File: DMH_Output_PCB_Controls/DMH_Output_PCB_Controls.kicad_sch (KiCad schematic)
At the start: 10 parts, among them J1 TS_Jack_6.35mm_Sw, J2 TS_Jack_6.35mm_Sw, J200 IDC_02x08, J3 TRS Jack 6.35mm, J4 TRS Jack 6.35mm, J5 TRS Jack 6.35mm, J6 TS_Jack_6.35mm_Sw, J7 TS_Jack_6.35mm_Sw, J8 TS_Jack_6.35mm_Sw, J9 TS_Jack_6.35mm_Sw

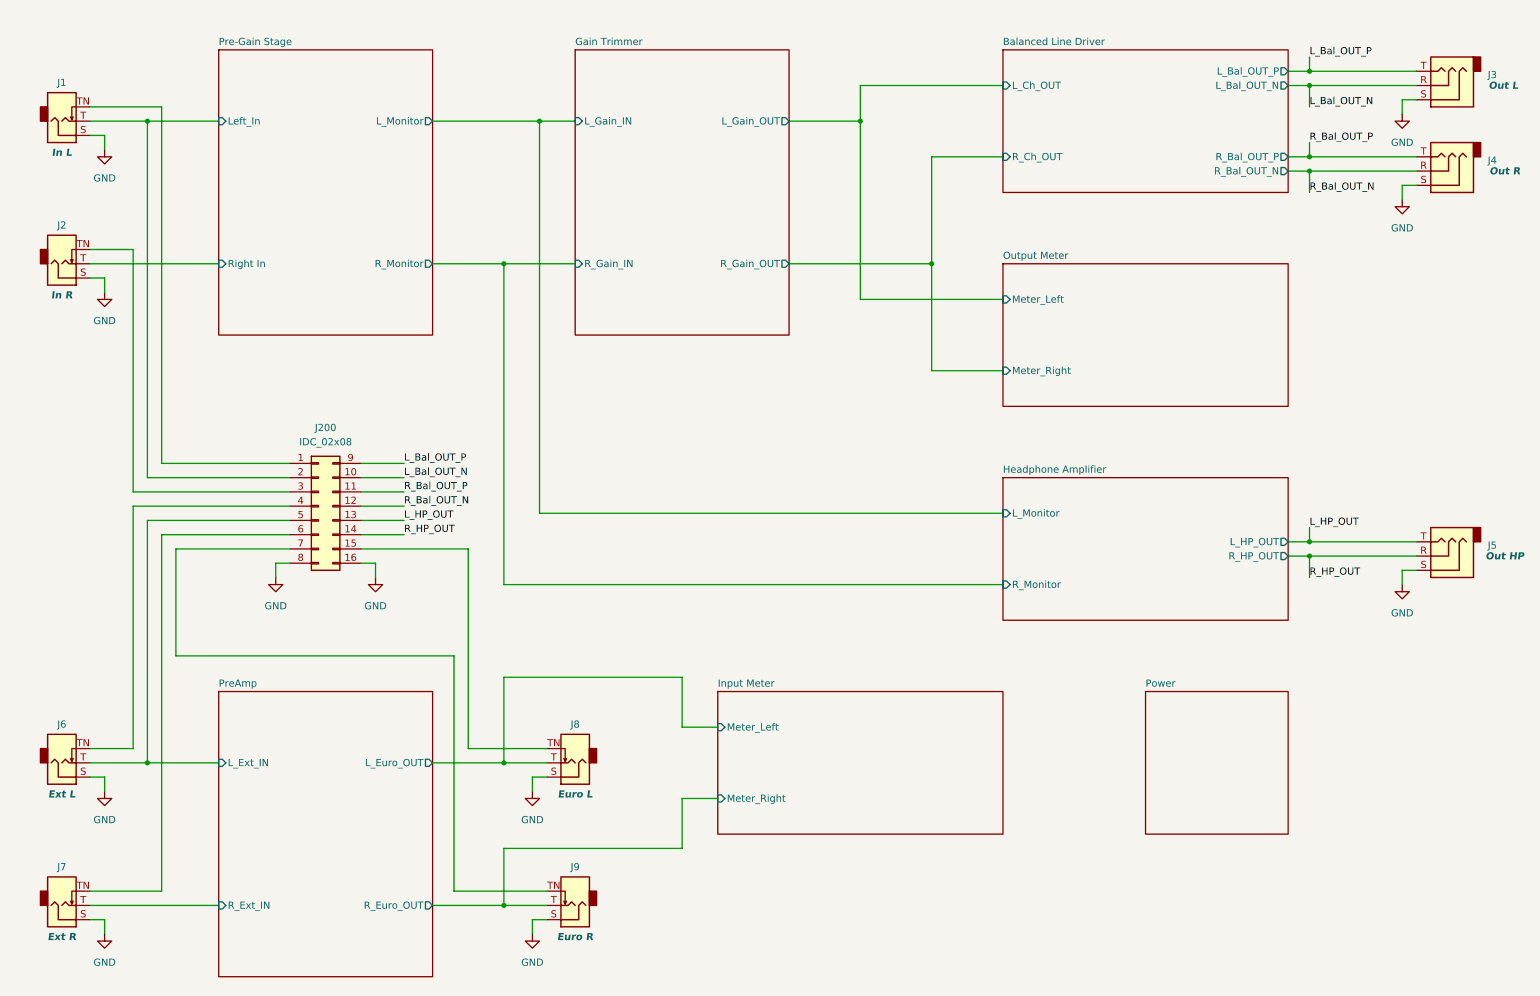
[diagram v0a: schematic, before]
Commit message: Controls PCB placement ongoing
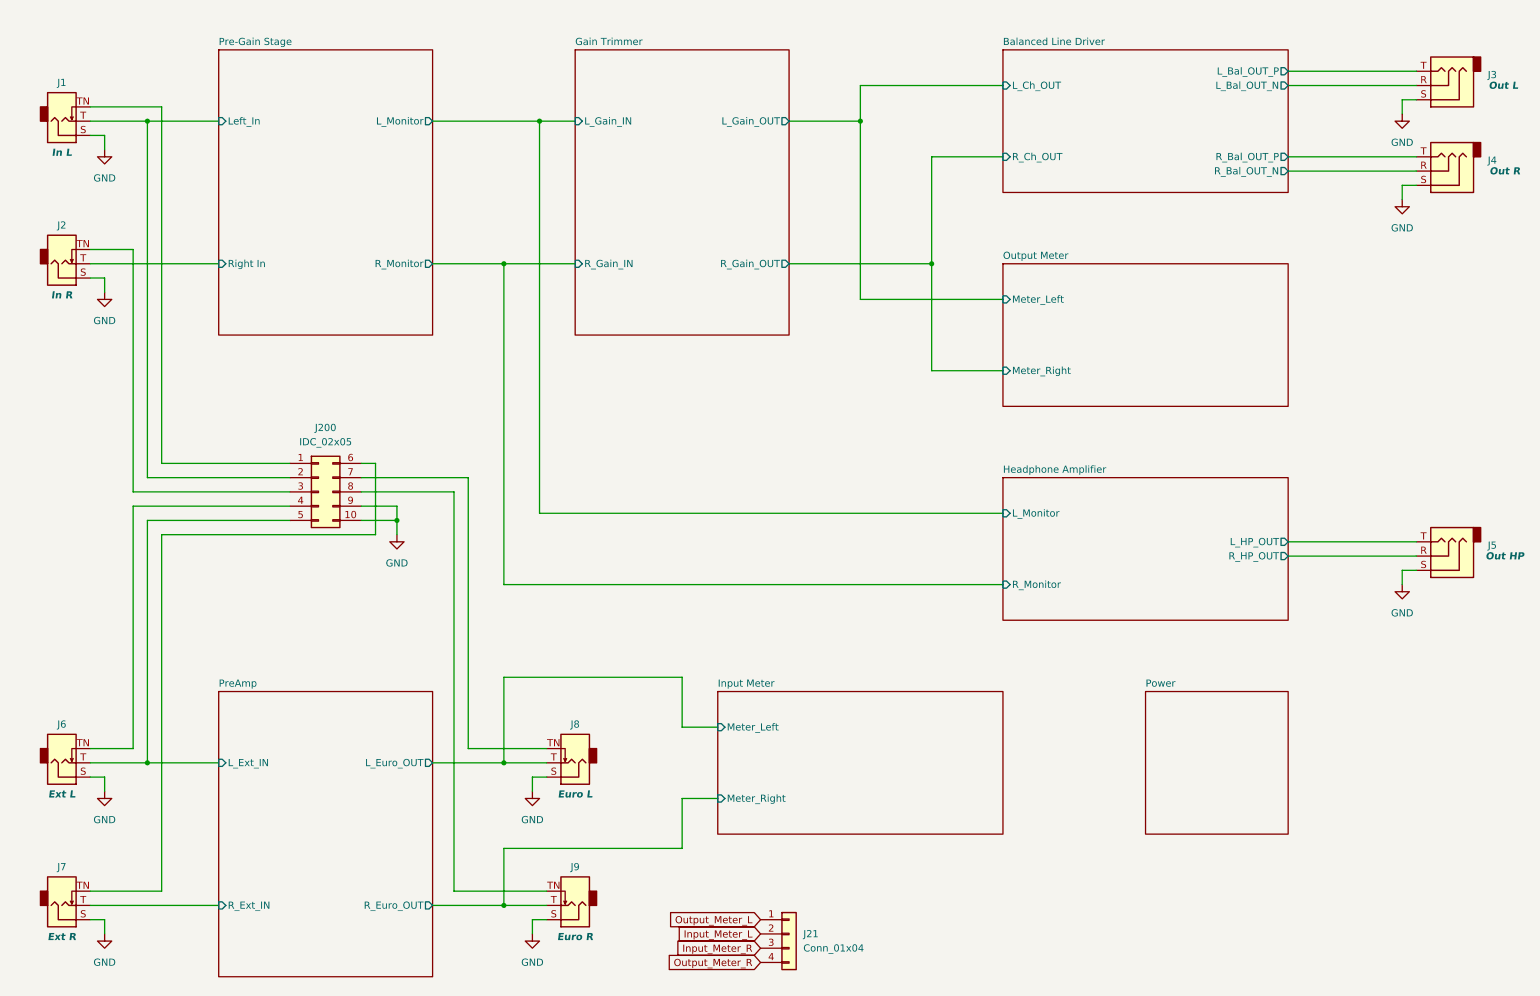
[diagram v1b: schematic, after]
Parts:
- removed J200: IDC_02x08, SynthStuff:IDC-Header_2x08_P2.54mm_Vertical_BackBone, symbol SynthStuff:BackBone_Connector_16Pin
- added J200: IDC_02x05, SynthStuff:IDC-Header_2x05_P2.54mm_Vertical_BackBone, symbol SynthStuff:BackBone_Connector_10Pin
- added J21: Conn_01x04, Connector_PinSocket_2.54mm:PinSocket_1x04_P2.54mm_Vertical, symbol Connector_Generic:Conn_01x04
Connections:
- net GND: now also J200.10 (Pin_10), J200.9 (Pin_9)
- net Pre-Gain Stage/Left_In: now also J200.2 (Pin_2)
- net PreAmp/L_Ext_IN: now also J200.5 (Pin_5)
- net at J8.TN: now also J200.7 (Pin_7)
- net at J2.TN: now also J200.3 (Pin_3)
- net at J7.TN: now also J200.6 (Pin_6)
- net at J6.TN: now also J200.4 (Pin_4)
- net at J1.TN: now also J200.1 (Pin_1)
- net at J9.TN: now also J200.8 (Pin_8)
- net L_Bal_OUT_N renamed Balanced Line Driver/L_Bal_OUT_N
- net L_Bal_OUT_P renamed Balanced Line Driver/L_Bal_OUT_P
- net L_HP_OUT renamed Headphone Amplifier/L_HP_OUT
- net R_Bal_OUT_N renamed Balanced Line Driver/R_Bal_OUT_N
- net R_Bal_OUT_P renamed Balanced Line Driver/R_Bal_OUT_P
- net R_HP_OUT renamed Headphone Amplifier/R_HP_OUT
- new net Input_Meter_L: J21.2 (Pin_2)
- new net Input_Meter_R: J21.3 (Pin_3)
- new net Output_Meter_L: J21.1 (Pin_1)
- new net Output_Meter_R: J21.4 (Pin_4)

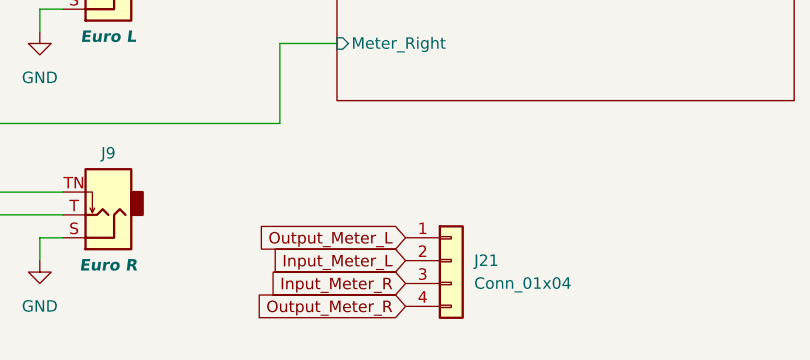
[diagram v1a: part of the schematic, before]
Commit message: Controls PCB routing ongoing
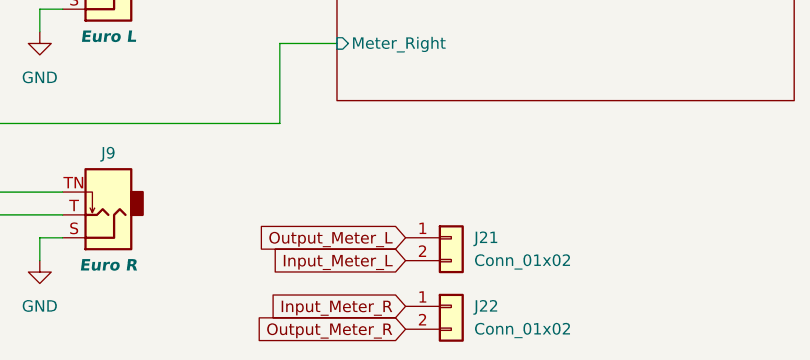
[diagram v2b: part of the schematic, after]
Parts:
- removed J21: Conn_01x04, Connector_PinSocket_2.54mm:PinSocket_1x04_P2.54mm_Vertical, symbol Connector_Generic:Conn_01x04
- added J21, J22: Conn_01x02, Connector_PinSocket_2.54mm:PinSocket_1x02_P2.54mm_Vertical, symbol Connector_Generic:Conn_01x02
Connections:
- net Input_Meter_L: now also J21.2 (Pin_2)
- net Input_Meter_R: now also J22.1 (Pin_1)
- net Output_Meter_L: now also J21.1 (Pin_1)
- net Output_Meter_R: now also J22.2 (Pin_2)
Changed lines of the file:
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@@
 	(global_label "Input_Meter_R"
 		(shape input)
-		(at 147.32 185.42 180)
+		(at 147.32 187.96 180)
 		(fields_autoplaced yes)
 		(effects
@@
 		)
 		(property "Intersheetrefs" "${INTERSHEET_REFS}"
-			(at 131.2116 185.42 0)
+			(at 131.2116 187.96 0)
 			(effects
 				(font
@@
 	(global_label "Output_Meter_R"
 		(shape input)
-		(at 147.32 187.96 180)
+		(at 147.32 190.5 180)
 		(fields_autoplaced yes)
 		(effects
@@
 		)
 		(property "Intersheetrefs" "${INTERSHEET_REFS}"
-			(at 129.7602 187.96 0)
+			(at 129.7602 190.5 0)
 			(effects
 				(font
@@
 	)
 	(symbol
-		(lib_id "Connector_Generic:Conn_01x04")
-		(at 152.4 182.88 0)
-		(unit 1)
-		(exclude_from_sim no)
-		(in_bom yes)
-		(on_board yes)
-		(dnp no)
-		(fields_autoplaced yes)
-		(property "Reference" "J21"
-			(at 154.94 182.8799 0)
-			(effects
-				(font
-					(size 1.27 1.27)
-				)
-				(justify left)
-			)
-		)
-		(property "Value" "Conn_01x04"
-			(at 154.94 185.4199 0)
-			(effects
-				(font
-					(size 1.27 1.27)
-				)
-				(justify left)
-			)
-		)
-		(property "Footprint" "Connector_PinSocket_2.54mm:PinSocket_1x04_P2.54mm_Vertical"
-			(at 152.4 182.88 0)
-			(effects
-				(font
-					(size 1.27 1.27)
-				)
-				(hide yes)
-			)
-		)
-		(property "Datasheet" "~"
-			(at 152.4 182.88 0)
-			(effects
-				(font
-					(size 1.27 1.27)
-				)
-				(hide yes)
-			)
-		)
-		(property "Description" "Generic connector, single row, 01x04, script generated (kicad-library-utils/schlib/autogen/connector/)"
-			(at 152.4 182.88 0)
-			(effects
-				(font
-					(size 1.27 1.27)
-				)
-				(hide yes)
-			)
-		)
-		(pin "2"
-		)
-		(pin "3"
-		)
-		(pin "4"
-		)
-		(pin "1"
-		)
-		(instances
-			(project ""
-				(path "/58f4306d-5387-4983-bb08-41a2313fd315"
-					(reference "J21")
-					(unit 1)
-				)
-			)
-		)
-	)
-	(symbol
 		(lib_id "SynthStuff:TS_Jack_6.35mm_Sw")
 		(at 22.86 63.5 0)
@@
 	)
 	(symbol
+		(lib_id "Connector_Generic:Conn_01x02")
+		(at 152.4 187.96 0)
+		(unit 1)
+		(exclude_from_sim no)
+		(in_bom yes)
+		(on_board yes)
+		(dnp no)
+		(fields_autoplaced yes)
+		(property "Reference" "J22"
+			(at 154.94 187.9599 0)
+			(effects
+				(font
+					(size 1.27 1.27)
+				)
+				(justify left)
+			)
+		)
+		(property "Value" "Conn_01x02"
+			(at 154.94 190.4999 0)
+			(effects
+				(font
+					(size 1.27 1.27)
+				)
+				(justify left)
+			)
+		)
+		(property "Footprint" "Connector_PinSocket_2.54mm:PinSocket_1x02_P2.54mm_Vertical"
+			(at 152.4 187.96 0)
+			(effects
+				(font
+					(size 1.27 1.27)
+				)
+				(hide yes)
+			)
+		)
+		(property "Datasheet" "~"
+			(at 152.4 187.96 0)
+			(effects
+				(font
+					(size 1.27 1.27)
+				)
+				(hide yes)
+			)
+		)
+		(property "Description" "Generic connector, single row, 01x02, script generated (kicad-library-utils/schlib/autogen/connector/)"
+			(at 152.4 187.96 0)
+			(effects
+				(font
+					(size 1.27 1.27)
+				)
+				(hide yes)
+			)
+		)
+		(pin "2"
+		)
+		(pin "1"
+		)
+		(instances
+			(project "DMH_Output_PCB_Controls"
+				(path "/58f4306d-5387-4983-bb08-41a2313fd315"
+					(reference "J22")
+					(unit 1)
+				)
+			)
+		)
+	)
+	(symbol
 		(lib_id "power:GND")
 		(at 261.62 52.07 0)
@@
 					(unit 1)
 				)
+			)
+		)
+	)
+	(symbol
+		(lib_id "Connector_Generic:Conn_01x02")
+		(at 152.4 180.34 0)
+		(unit 1)
+		(exclude_from_sim no)
+		(in_bom yes)
+		(on_board yes)
+		(dnp no)
+		(fields_autoplaced yes)
+		(property "Reference" "J21"
+			(at 154.94 180.3399 0)
+			(effects
+				(font
+					(size 1.27 1.27)
+				)
+				(justify left)
+			)
+		)
+		(property "Value" "Conn_01x02"
+			(at 154.94 182.8799 0)
+			(effects
+				(font
+					(size 1.27 1.27)
+				)
+				(justify left)
+			)
+		)
+		(property "Footprint" "Connector_PinSocket_2.54mm:PinSocket_1x02_P2.54mm_Vertical"
+			(at 152.4 180.34 0)
+			(effects
+				(font
+					(size 1.27 1.27)
+				)
+				(hide yes)
+			)
+		)
+		(property "Datasheet" "~"
+			(at 152.4 180.34 0)
+			(effects
+				(font
+					(size 1.27 1.27)
+				)
+				(hide yes)
+			)
+		)
+		(property "Description" "Generic connector, single row, 01x02, script generated (kicad-library-utils/schlib/autogen/connector/)"
+			(at 152.4 180.34 0)
+			(effects
+				(font
+					(size 1.27 1.27)
+				)
+				(hide yes)
+			)
+		)
+		(pin "2"
+		)
+		(pin "1"
+		)
+		(instances
+			(project ""
+				(path "/58f4306d-5387-4983-bb08-41a2313fd315"
+					(reference "J21")
+					(unit 1)
+				)

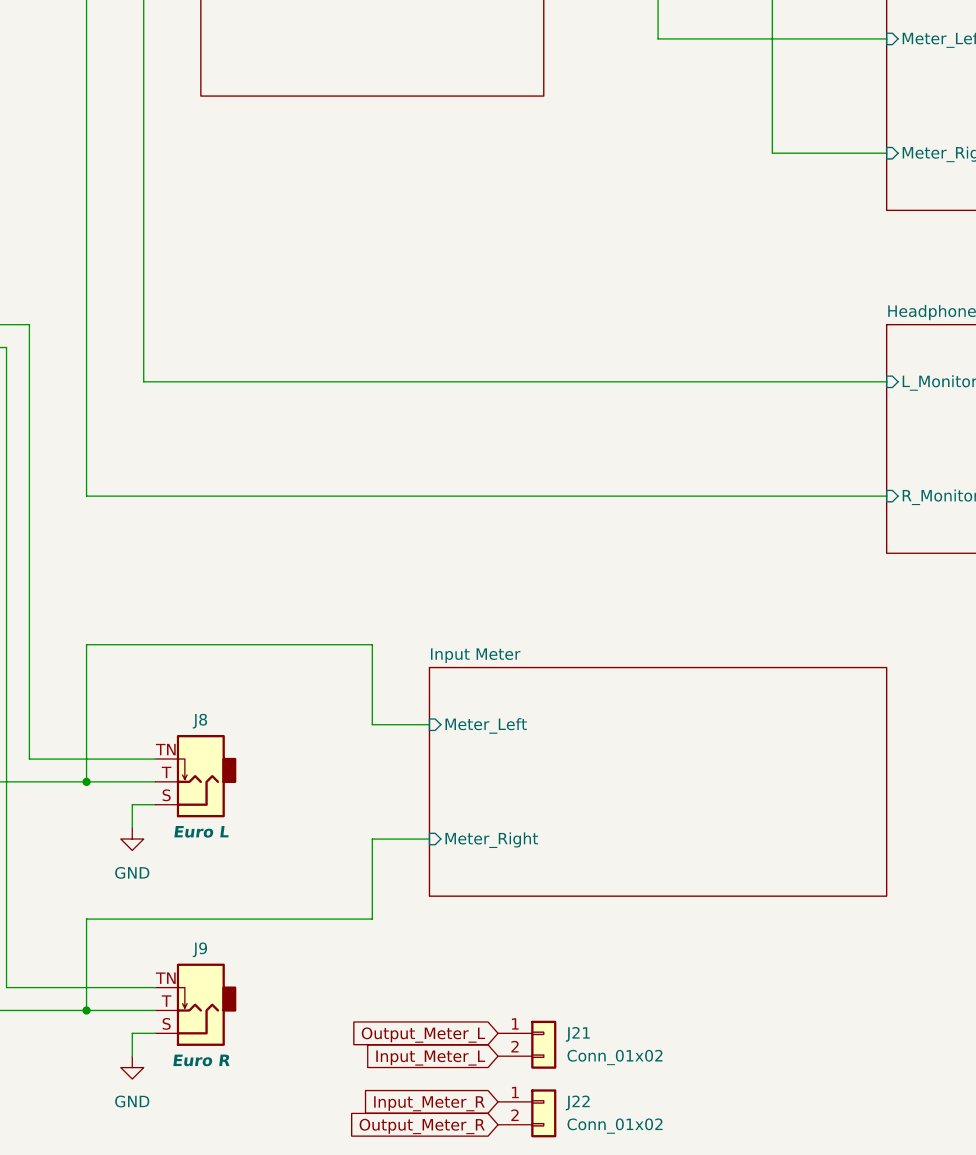
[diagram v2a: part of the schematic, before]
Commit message: Clarifying inter PCB connectors in progress
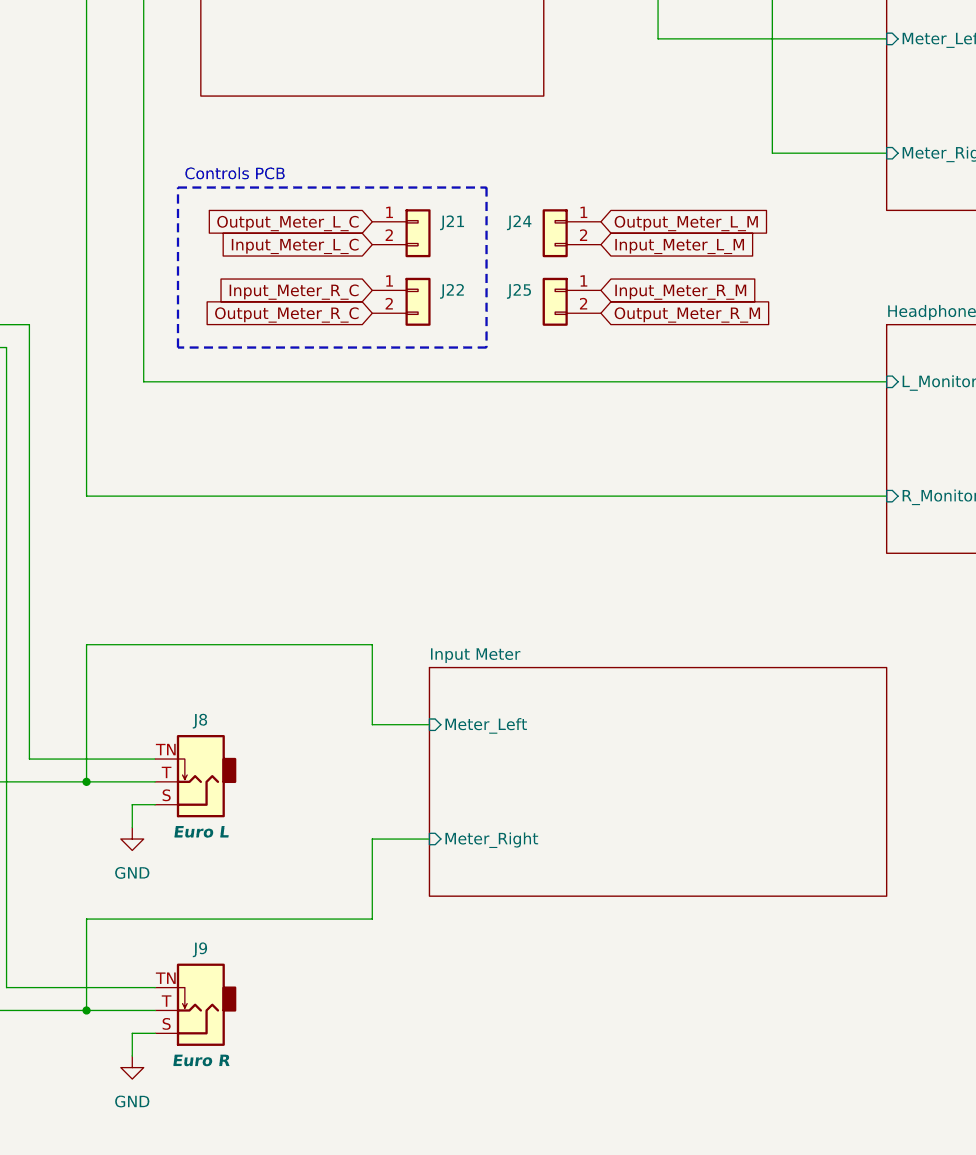
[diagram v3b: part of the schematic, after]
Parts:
- added J24, J25: Conn_01x02, Connector_PinSocket_2.54mm:PinSocket_1x02_P2.54mm_Vertical, symbol Connector_Generic:Conn_01x02
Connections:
- net Input_Meter_L renamed Input_Meter_L_C
- net Input_Meter_R renamed Input_Meter_R_C
- net Output_Meter_L renamed Output_Meter_L_C
- net Output_Meter_R renamed Output_Meter_R_C
- new net Input_Meter_L_M: J24.2 (Pin_2)
- new net Input_Meter_R_M: J25.1 (Pin_1)
- new net Output_Meter_L_M: J24.1 (Pin_1)
- new net Output_Meter_R_M: J25.2 (Pin_2)
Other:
- note added: "Controls PCB"
- moved on the sheet: J21, J22

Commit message: Controls PCB routing in progress
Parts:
- J24, J25: footprint Connector_PinSocket_2.54mm:PinSocket_1x02_P2.54mm_Vertical -> Connector_PinHeader_2.54mm:PinHeader_1x02_P2.54mm_Vertical
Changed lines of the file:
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@@
 		(exclude_from_sim no)
 		(in_bom yes)
-		(on_board yes)
+		(on_board no)
 		(dnp no)
 		(fields_autoplaced yes)
@@
 			)
 		)
-		(property "Footprint" "Connector_PinSocket_2.54mm:PinSocket_1x02_P2.54mm_Vertical"
+		(property "Footprint" "Connector_PinHeader_2.54mm:PinHeader_1x02_P2.54mm_Vertical"
 			(at 153.67 97.79 0)
 			(effects
@@
 				)
 				(hide yes)
+			)
+		)
+		(property "Function" ""
+			(at 153.67 97.79 0)
+			(effects
+				(font
+					(size 1.27 1.27)
+				)
 			)
 		)
@@
 		(exclude_from_sim no)
 		(in_bom yes)
-		(on_board yes)
+		(on_board no)
 		(dnp no)
 		(fields_autoplaced yes)
@@
 			)
 		)
-		(property "Footprint" "Connector_PinSocket_2.54mm:PinSocket_1x02_P2.54mm_Vertical"
+		(property "Footprint" "Connector_PinHeader_2.54mm:PinHeader_1x02_P2.54mm_Vertical"
 			(at 153.67 90.17 0)
 			(effects
@@
 			)
 		)
+		(property "Function" ""
+			(at 153.67 90.17 0)
+			(effects
+				(font
+					(size 1.27 1.27)
+				)
+			)
+		)
